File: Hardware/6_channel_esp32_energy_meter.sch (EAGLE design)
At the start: 117 parts, among them IC1 ATM90E32AS, IC2 ATM90E32AS, IC3 LMR14020SDDA, J16 PINHD-1X19, J4 9-12VAC, J5 PINHD1X1-SM1X01_SM, J6 PINHD1X1-SM1X01_SM, J8 PINHD1X1-SM1X01_SM, U1 ESP32-DEVKITC-32D, Y1 16.384MHz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

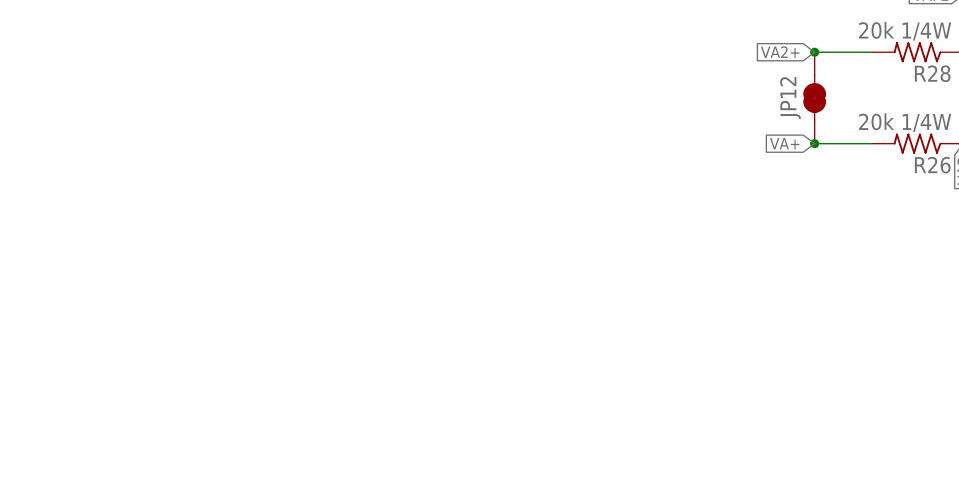
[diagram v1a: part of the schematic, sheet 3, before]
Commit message: v1.4
- Added optional micro-hdmi connection to connect the current transformer remote board. This allows for all 6 current transformer connections to connect to a remote pcb, which then connects to the main board via 1 micro-hdmi cable. Instead of 6 wires coming out of the meter, there can now be 1.
- Added current transformer remote pcb
- Removed JP8-JP11 and connected all voltage channels together for each ATM90E32
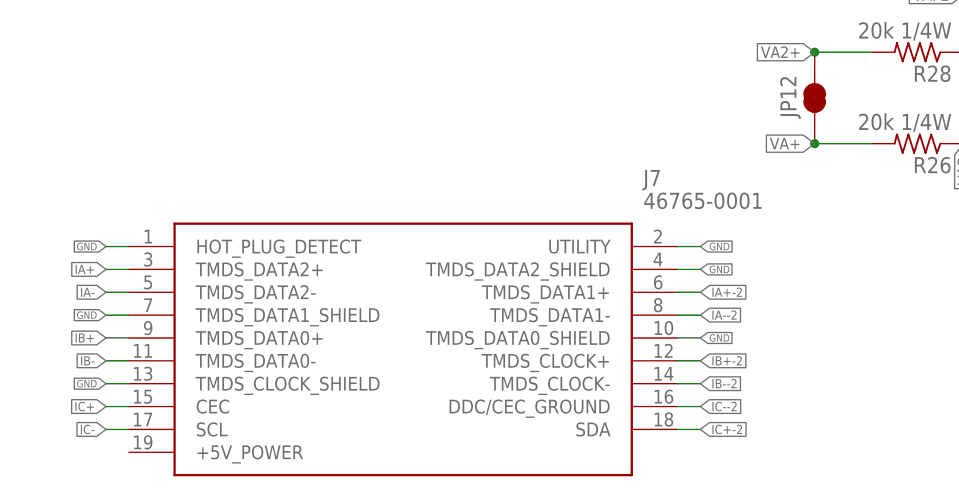
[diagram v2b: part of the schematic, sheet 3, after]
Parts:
- removed JP10, JP11, JP8, JP9: JUMPER-SMT_3_NO_SILK, SparkFun-Jumpers:JUMPER-SMT_3_NO_SILK
- added J7: 46765-0001, 46765-0001:46765-0001
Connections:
- removed net V2N: IC1.V2N, JP9.3
- removed net V2N-2: IC2.V2N, JP11.3
- removed net V2P: IC1.V2P, JP8.3
- removed net V2P-2: IC2.V2P, JP10.3
- removed net V3N: IC1.V3N, JP9.1
- removed net V3N-2: IC2.V3N, JP11.1
- removed net V3P: IC1.V3P, JP8.1
- removed net V3P-2: IC2.V3P, JP10.1
- net GND: now also J7.HOT_PLUG_DETECT, J7.TMDS_CLOCK_SHIELD, J7.TMDS_DATA0_SHIELD, J7.TMDS_DATA1_SHIELD, J7.TMDS_DATA2_SHIELD, J7.UTILITY
- net IA+: now also J7.TMDS_DATA2+
- net IA+-2: now also J7.TMDS_DATA1+
- net IA-: now also J7.TMDS_DATA2-
- net IA--2: now also J7.TMDS_DATA1-
- net IB+: now also J7.TMDS_DATA0+
- net IB+-2: now also J7.TMDS_CLOCK+
- net IB-: now also J7.TMDS_DATA0-
- net IB--2: now also J7.TMDS_CLOCK-
- net IC+: now also J7.CEC
- net IC+-2: now also J7.SDA
- net IC-: now also J7.SCL
- net IC--2: now also J7.DDC/CEC_GROUND
- net VAN: now also IC1.V2N, IC1.V3N; no longer JP9.2
- net VAN2: now also IC2.V2N, IC2.V3N; no longer JP11.2
- net VAP: now also IC1.V2P, IC1.V3P; no longer JP8.2
- net VAP2: now also IC2.V2P, IC2.V3P; no longer JP10.2

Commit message: v1.4 rev1
- Changed micro-hdmi connector to through-hole
- Changed spacing on VA2+/VA2- (voltage 2 connection) to 3.5mm to allow for standard screw connectors
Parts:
- removed J7: 46765-0001, 46765-0001:46765-0001
- added J9: PKS019-4011-0, SamacSys_Parts:PKS019-4011-0
- D1: value 500mV 3A -> (none); device SamacSys_Parts:B340A-13-FSMA -> diode:DIODE-DO214AC
- J3: device SparkFun-Connectors:CONN_02 -> SparkFun-Connectors:CONN_023.5MM
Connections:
- net GND: now also BR1.~, J9.1, J9.10, J9.11, J9.14, J9.19, J9.20, J9.21, J9.22, J9.23, J9.4, J9.7; no longer BR1.~_2, J7.HOT_PLUG_DETECT, J7.TMDS_CLOCK_SHIELD, J7.TMDS_DATA0_SHIELD, J7.TMDS_DATA1_SHIELD, J7.TMDS_DATA2_SHIELD, J7.UTILITY
- net IA+: now also J9.2; no longer J7.TMDS_DATA2+
- net IA+-2: now also J9.12; no longer J7.TMDS_DATA1+
- net IA-: now also J9.3; no longer J7.TMDS_DATA2-
- net IA--2: now also J9.13; no longer J7.TMDS_DATA1-
- net IB+: now also J9.5; no longer J7.TMDS_DATA0+
- net IB+-2: now also J9.15; no longer J7.TMDS_CLOCK+
- net IB-: now also J9.6; no longer J7.TMDS_DATA0-
- net IB--2: now also J9.16; no longer J7.TMDS_CLOCK-
- net IC+: now also J9.8; no longer J7.CEC
- net IC+-2: now also J9.18; no longer J7.SDA
- net IC-: now also J9.9; no longer J7.SCL
- net IC--2: now also J9.17; no longer J7.DDC/CEC_GROUND
- net SW: now also D1.C; no longer D1.K
- net VA2+: now also J3.2; no longer J3.1
- net VA2-: now also J3.1; no longer J3.2
- net VIN: now also BR1.~1; no longer BR1.~_1

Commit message: Updated Eagle files to v1.4 rev1
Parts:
- C17, C18, C19, C2, C20, C21, C22, C3, C4, C5, C6, C7: value .33uF -> 18nf
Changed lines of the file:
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@@
 <?xml version="1.0" encoding="utf-8"?>
 <!DOCTYPE eagle SYSTEM "eagle.dtd">
-<eagle version="9.5.1">
+<eagle version="9.6.2">
 <drawing>
 <settings>
-<setting alwaysvectorfont="no"/>
+<setting alwaysvectorfont="yes"/>
 <setting keepoldvectorfont="yes"/>
 <setting verticaltext="up"/>
@@
 <part name="FRAME1" library="SparkFun-Aesthetics" library_urn="urn:adsk.eagle:library:507" deviceset="FRAME-A4L" device=""/>
 <part name="R7" library="rcl" library_urn="urn:adsk.eagle:library:334" deviceset="R-US_" device="R0603" package3d_urn="urn:adsk.eagle:package:23555/3" value="22"/>
-<part name="C2" library="rcl" library_urn="urn:adsk.eagle:library:334" deviceset="C-US" device="C0603" package3d_urn="urn:adsk.eagle:package:23616/2" value=".33uF"/>
-<part name="C3" library="rcl" library_urn="urn:adsk.eagle:library:334" deviceset="C-US" device="C0603" package3d_urn="urn:adsk.eagle:package:23616/2" value=".33uF"/>
+<part name="C2" library="rcl" library_urn="urn:adsk.eagle:library:334" deviceset="C-US" device="C0603" package3d_urn="urn:adsk.eagle:package:23616/2" value="18nf"/>
+<part name="C3" library="rcl" library_urn="urn:adsk.eagle:library:334" deviceset="C-US" device="C0603" package3d_urn="urn:adsk.eagle:package:23616/2" value="18nf"/>
 <part name="R8" library="rcl" library_urn="urn:adsk.eagle:library:334" deviceset="R-US_" device="R0603" package3d_urn="urn:adsk.eagle:package:23555/3" value="22"/>
-<part name="C4" library="rcl" library_urn="urn:adsk.eagle:library:334" deviceset="C-US" device="C0603" package3d_urn="urn:adsk.eagle:package:23616/2" value=".33uF"/>
-<part name="C5" library="rcl" library_urn="urn:adsk.eagle:library:334" deviceset="C-US" device="C0603" package3d_urn="urn:adsk.eagle:package:23616/2" value=".33uF"/>
+<part name="C4" library="rcl" library_urn="urn:adsk.eagle:library:334" deviceset="C-US" device="C0603" package3d_urn="urn:adsk.eagle:package:23616/2" value="18nf"/>
+<part name="C5" library="rcl" library_urn="urn:adsk.eagle:library:334" deviceset="C-US" device="C0603" package3d_urn="urn:adsk.eagle:package:23616/2" value="18nf"/>
 <part name="IC1" library="ATM90E36" deviceset="ATM90E36" device="" package3d_urn="urn:adsk.eagle:package:8170723/1" value="ATM90E32AS">
 <attribute name="SPICEPREFIX" value="X"/>
@@
 <part name="C10" library="rcl" library_urn="urn:adsk.eagle:library:334" deviceset="C-US" device="C0603" package3d_urn="urn:adsk.eagle:package:23616/2" value="0.1uF"/>
 <part name="R6" library="rcl" library_urn="urn:adsk.eagle:library:334" deviceset="R-US_" device="R0603" package3d_urn="urn:adsk.eagle:package:23555/3" value="22"/>
-<part name="C6" library="rcl" library_urn="urn:adsk.eagle:library:334" deviceset="C-US" device="C0603" package3d_urn="urn:adsk.eagle:package:23616/2" value=".33uF"/>
-<part name="C7" library="rcl" library_urn="urn:adsk.eagle:library:334" deviceset="C-US" device="C0603" package3d_urn="urn:adsk.eagle:package:23616/2" value=".33uF"/>
+<part name="C6" library="rcl" library_urn="urn:adsk.eagle:library:334" deviceset="C-US" device="C0603" package3d_urn="urn:adsk.eagle:package:23616/2" value="18nf"/>
+<part name="C7" library="rcl" library_urn="urn:adsk.eagle:library:334" deviceset="C-US" device="C0603" package3d_urn="urn:adsk.eagle:package:23616/2" value="18nf"/>
 <part name="GND3" library="SparkFun-Aesthetics" library_urn="urn:adsk.eagle:library:507" deviceset="GND" device=""/>
 <part name="JP3" library="SparkFun-Jumpers" library_urn="urn:adsk.eagle:library:528" deviceset="JUMPER-SMT_2_NC_TRACE" device="_SILK" package3d_urn="urn:adsk.eagle:package:39281/1" value=""/>
@@
 <part name="ZX0" library="wirepad" library_urn="urn:adsk.eagle:library:412" deviceset="WIREPAD" device="SMD1,27-254" package3d_urn="urn:adsk.eagle:package:30839/1"/>
 <part name="R18" library="rcl" library_urn="urn:adsk.eagle:library:334" deviceset="R-US_" device="R0603" package3d_urn="urn:adsk.eagle:package:23555/3" value="22"/>
-<part name="C17" library="rcl" library_urn="urn:adsk.eagle:library:334" deviceset="C-US" device="C0603" package3d_urn="urn:adsk.eagle:package:23616/2" value=".33uF"/>
-<part name="C18" library="rcl" library_urn="urn:adsk.eagle:library:334" deviceset="C-US" device="C0603" package3d_urn="urn:adsk.eagle:package:23616/2" value=".33uF"/>
+<part name="C17" library="rcl" library_urn="urn:adsk.eagle:library:334" deviceset="C-US" device="C0603" package3d_urn="urn:adsk.eagle:package:23616/2" value="18nf"/>
+<part name="C18" library="rcl" library_urn="urn:adsk.eagle:library:334" deviceset="C-US" device="C0603" package3d_urn="urn:adsk.eagle:package:23616/2" value="18nf"/>
 <part name="R19" library="rcl" library_urn="urn:adsk.eagle:library:334" deviceset="R-US_" device="R0603" package3d_urn="urn:adsk.eagle:package:23555/3" value="22"/>
-<part name="C19" library="rcl" library_urn="urn:adsk.eagle:library:334" deviceset="C-US" device="C0603" package3d_urn="urn:adsk.eagle:package:23616/2" value=".33uF"/>
-<part name="C20" library="rcl" library_urn="urn:adsk.eagle:library:334" deviceset="C-US" device="C0603" package3d_urn="urn:adsk.eagle:package:23616/2" value=".33uF"/>
+<part name="C19" library="rcl" library_urn="urn:adsk.eagle:library:334" deviceset="C-US" device="C0603" package3d_urn="urn:adsk.eagle:package:23616/2" value="18nf"/>
+<part name="C20" library="rcl" library_urn="urn:adsk.eagle:library:334" deviceset="C-US" device="C0603" package3d_urn="urn:adsk.eagle:package:23616/2" value="18nf"/>
 <part name="IC2" library="ATM90E36" deviceset="ATM90E36" device="" package3d_urn="urn:adsk.eagle:package:8170723/1" value="ATM90E32AS">
 <attribute name="SPICEPREFIX" value="X"/>
@@
 <part name="C25" library="rcl" library_urn="urn:adsk.eagle:library:334" deviceset="C-US" device="C0603" package3d_urn="urn:adsk.eagle:package:23616/2" value="0.1uF"/>
 <part name="R17" library="rcl" library_urn="urn:adsk.eagle:library:334" deviceset="R-US_" device="R0603" package3d_urn="urn:adsk.eagle:package:23555/3" value="22"/>
-<part name="C21" library="rcl" library_urn="urn:adsk.eagle:library:334" deviceset="C-US" device="C0603" package3d_urn="urn:adsk.eagle:package:23616/2" value=".33uF"/>
-<part name="C22" library="rcl" library_urn="urn:adsk.eagle:library:334" deviceset="C-US" device="C0603" package3d_urn="urn:adsk.eagle:package:23616/2" value=".33uF"/>
+<part name="C21" library="rcl" library_urn="urn:adsk.eagle:library:334" deviceset="C-US" device="C0603" package3d_urn="urn:adsk.eagle:package:23616/2" value="18nf"/>
+<part name="C22" library="rcl" library_urn="urn:adsk.eagle:library:334" deviceset="C-US" device="C0603" package3d_urn="urn:adsk.eagle:package:23616/2" value="18nf"/>
 <part name="GND14" library="SparkFun-Aesthetics" library_urn="urn:adsk.eagle:library:507" deviceset="GND" device=""/>
 <part name="JP6" library="SparkFun-Jumpers" library_urn="urn:adsk.eagle:library:528" deviceset="JUMPER-SMT_2_NC_TRACE" device="_SILK" package3d_urn="urn:adsk.eagle:package:39281/1" value=""/>
